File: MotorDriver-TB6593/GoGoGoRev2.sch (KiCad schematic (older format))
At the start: 17 parts, among them P2 CONN_01X04, P3 CONN_01X02, U1 TB6593FNG

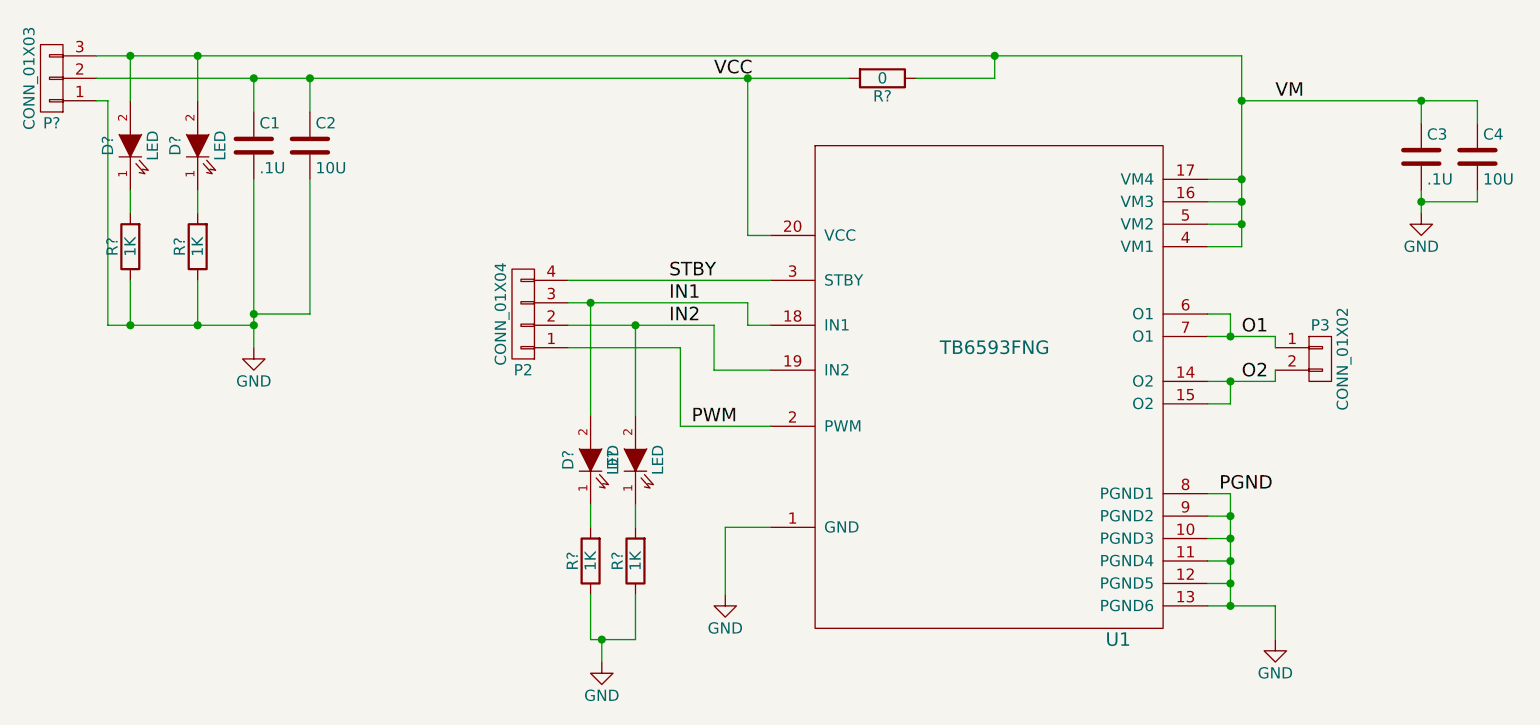
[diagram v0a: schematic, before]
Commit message: Finished layout, still need via stitching and DRC/DFM checks
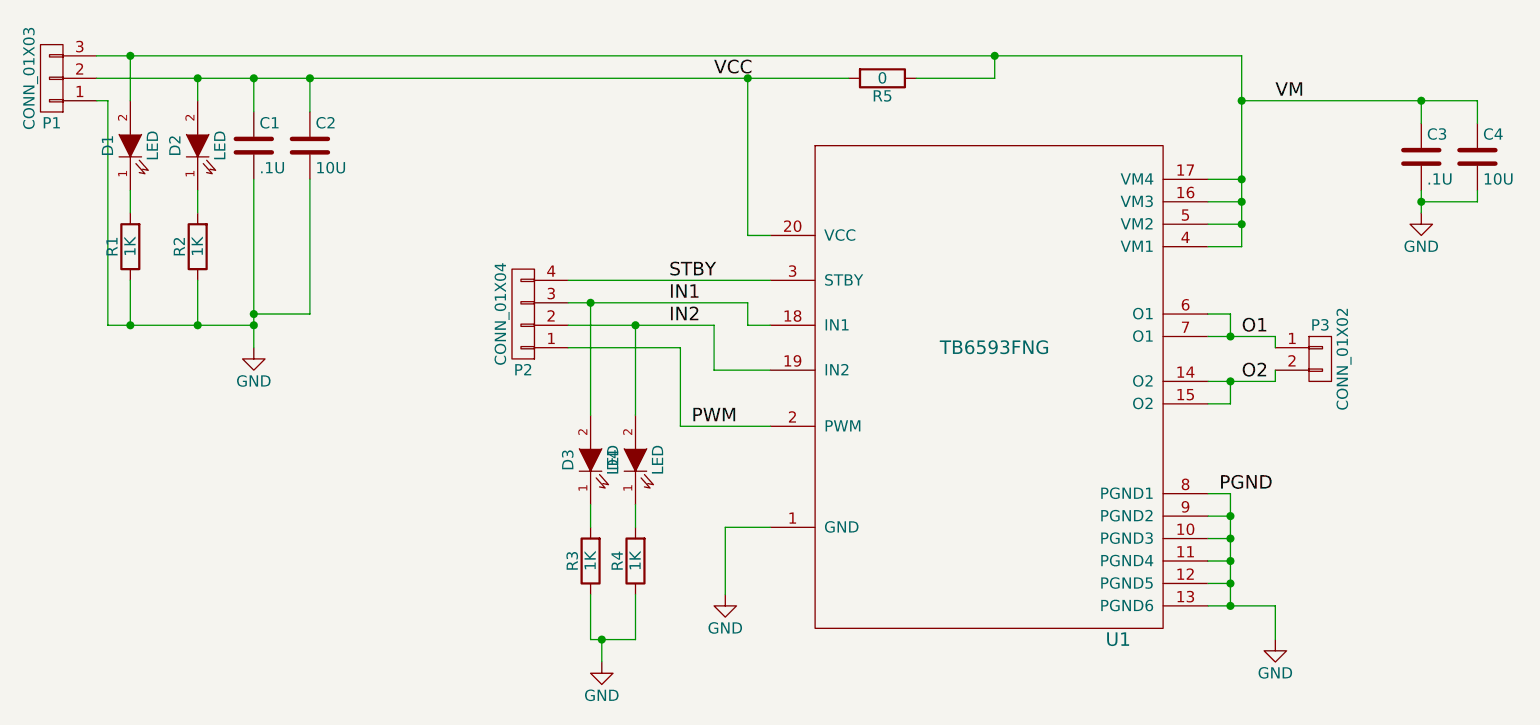
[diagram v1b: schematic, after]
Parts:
- D1, D2, D3, D4: renamed from D?; footprint (none) -> LEDs:LED-0805
- P1: renamed from P?; footprint (none) -> Pin_Headers:Pin_Header_Straight_1x03
- R1, R2, R3, R4, R5: renamed from R?; footprint (none) -> Resistors_SMD:R_0805_HandSoldering
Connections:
- net VCC: now also D2.2 (A)
- net VM: no longer D2.2 (A)
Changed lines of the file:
@@
 PGND
 $Comp
-L CONN_01X03 P?
+L CONN_01X03 P1
 U 1 1 56118A1D
 P 1650 1900
-F 0 "P?" H 1650 2100 50  0000 C CNN
+F 0 "P1" H 1650 2100 50  0000 C CNN
 F 1 "CONN_01X03" V 1750 1900 50  0000 C CNN
-F 2 "" H 1650 1900 60  0000 C CNN
+F 2 "Pin_Headers:Pin_Header_Straight_1x03" H 1650 1900 60  0001 C CNN
 F 3 "" H 1650 1900 60  0000 C CNN
 	1    1650 1900
@@
 Connection ~ 6950 2000
 $Comp
-L R R?
+L R R5
 U 1 1 56118B07
 P 5350 1900
-F 0 "R?" V 5430 1900 50  0000 C CNN
+F 0 "R5" V 5430 1900 50  0000 C CNN
 F 1 "0" V 5350 1900 50  0000 C CNN
-F 2 "" V 5280 1900 30  0000 C CNN
+F 2 "Resistors_SMD:R_0805_HandSoldering" V 5280 1900 30  0001 C CNN
 F 3 "" H 5350 1900 30  0000 C CNN
 	1    5350 1900
@@
 Connection ~ 5850 1800
 $Comp
-L LED D?
+L LED D1
 U 1 1 56119242
 P 2000 2200
-F 0 "D?" H 2000 2300 50  0000 C CNN
+F 0 "D1" H 2000 2300 50  0000 C CNN
 F 1 "LED" H 2000 2100 50  0000 C CNN
-F 2 "" H 2000 2200 60  0000 C CNN
+F 2 "LEDs:LED-0805" H 2000 2200 60  0001 C CNN
 F 3 "" H 2000 2200 60  0000 C CNN
 	1    2000 2200
-	0    -1   -1   0
-$EndComp
-$Comp
-L LED D?
-U 1 1 56119293
-P 2300 2200
-F 0 "D?" H 2300 2300 50  0000 C CNN
-F 1 "LED" H 2300 2100 50  0000 C CNN
-F 2 "" H 2300 2200 60  0000 C CNN
-F 3 "" H 2300 2200 60  0000 C CNN
-	1    2300 2200
 	0    -1   -1   0
 $EndComp
@@
 	2000 2000 2000 1800
 Connection ~ 2000 1800
-Wire Wire Line
-	2300 2000 2300 1800
-Connection ~ 2300 1800
 $Comp
-L R R?
+L R R1
 U 1 1 5611956C
 P 2000 2650
-F 0 "R?" V 2080 2650 50  0000 C CNN
+F 0 "R1" V 2080 2650 50  0000 C CNN
 F 1 "1K" V 2000 2650 50  0000 C CNN
-F 2 "" V 1930 2650 30  0000 C CNN
+F 2 "Resistors_SMD:R_0805_HandSoldering" V 1930 2650 30  0001 C CNN
 F 3 "" H 2000 2650 30  0000 C CNN
 	1    2000 2650
@@
 Connection ~ 2000 3000
 $Comp
-L R R?
+L R R2
 U 1 1 56119778
 P 2300 2650
-F 0 "R?" V 2380 2650 50  0000 C CNN
+F 0 "R2" V 2380 2650 50  0000 C CNN
 F 1 "1K" V 2300 2650 50  0000 C CNN
-F 2 "" V 2230 2650 30  0000 C CNN
+F 2 "Resistors_SMD:R_0805_HandSoldering" V 2230 2650 30  0001 C CNN
 F 3 "" H 2300 2650 30  0000 C CNN
 	1    2300 2650
@@
 Connection ~ 2300 3000
 $Comp
-L LED D?
+L LED D3
 U 1 1 56119A84
 P 4050 3600
-F 0 "D?" H 4050 3700 50  0000 C CNN
+F 0 "D3" H 4050 3700 50  0000 C CNN
 F 1 "LED" H 4050 3500 50  0000 C CNN
-F 2 "" H 4050 3600 60  0000 C CNN
+F 2 "LEDs:LED-0805" H 4050 3600 60  0001 C CNN
 F 3 "" H 4050 3600 60  0000 C CNN
 	1    4050 3600
@@
 	4050 2900 4050 3400
 $Comp
-L R R?
+L R R3
 U 1 1 56119A8B
 P 4050 4050
-F 0 "R?" V 4130 4050 50  0000 C CNN
+F 0 "R3" V 4130 4050 50  0000 C CNN
 F 1 "1K" V 4050 4050 50  0000 C CNN
-F 2 "" V 3980 4050 30  0000 C CNN
+F 2 "Resistors_SMD:R_0805_HandSoldering" V 3980 4050 30  0001 C CNN
 F 3 "" H 4050 4050 30  0000 C CNN
 	1    4050 4050
@@
 	4050 4200 4050 4400
 $Comp
-L LED D?
+L LED D4
 U 1 1 56119AF3
 P 4250 3600
-F 0 "D?" H 4250 3700 50  0000 C CNN
+F 0 "D4" H 4250 3700 50  0000 C CNN
 F 1 "LED" H 4250 3500 50  0000 C CNN
-F 2 "" H 4250 3600 60  0000 C CNN
+F 2 "LEDs:LED-0805" H 4250 3600 60  0001 C CNN
 F 3 "" H 4250 3600 60  0000 C CNN
 	1    4250 3600
@@
 	4250 3000 4250 3400
 $Comp
-L R R?
+L R R4
 U 1 1 56119AFA
 P 4250 4050
-F 0 "R?" V 4330 4050 50  0000 C CNN
+F 0 "R4" V 4330 4050 50  0000 C CNN
 F 1 "1K" V 4250 4050 50  0000 C CNN
-F 2 "" V 4180 4050 30  0000 C CNN
+F 2 "Resistors_SMD:R_0805_HandSoldering" V 4180 4050 30  0001 C CNN
 F 3 "" H 4250 4050 30  0000 C CNN
 	1    4250 4050
@@
 	4250 4400 4050 4400
 $Comp
-L GND #PWR?
+L GND #PWR05
 U 1 1 56119EE1
 P 4100 4500
-F 0 "#PWR?" H 4100 4250 50  0001 C CNN
+F 0 "#PWR05" H 4100 4250 50  0001 C CNN
 F 1 "GND" H 4100 4350 50  0000 C CNN
 F 2 "" H 4100 4500 60  0000 C CNN
@@
 	4100 4500 4100 4400
 Connection ~ 4100 4400
+$Comp
+L LED D2
+U 1 1 56119293
+P 2300 2200
+F 0 "D2" H 2300 2300 50  0000 C CNN
+F 1 "LED" H 2300 2100 50  0000 C CNN
+F 2 "LEDs:LED-0805" H 2300 2200 60  0001 C CNN
+F 3 "" H 2300 2200 60  0000 C CNN
+	1    2300 2200
+	0    -1   -1   0
+$EndComp
+Wire Wire Line
+	2300 1900 2300 2000
+Connection ~ 2300 1900
 $EndSCHEMATC
